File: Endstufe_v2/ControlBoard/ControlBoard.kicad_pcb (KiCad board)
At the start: 2 copper layers, 216 parts, among them J1 B4B-XH-2_(LF)(SN), J10 DNP, J11 DNP, J12 DNP, J13 DNP, J14 DAC all outputs, J2 B4B-XH-2_(LF)(SN), J3 B4B-XH-2_(LF)(SN), J4 DNP, J5 B6B-XH-2(LF)(SN), J6 Conn_01x02_Pin, J7 DNP, J8 DNP, J9 DNP, SW1 TS-1187A-B-A-B, SW2 TS-1187A-B-A-B, U1 NVTFWS014P04M8LTAG, U10 ADAU1962AWBSTZ, U2 1SMA5927A, U3 TPS62933, U4 TYPE-C 16PFS 2JCB1.2-H6.5 IPX8, U5 W25Q128JVS, U6 RP2040, U7 W25Q128JVS, U8 ADAU1463WBCPZ300, U9 ZPLR135_T8, Y1 12Mhz, Y2 24.576Mhz, Y3 24.576Mhz

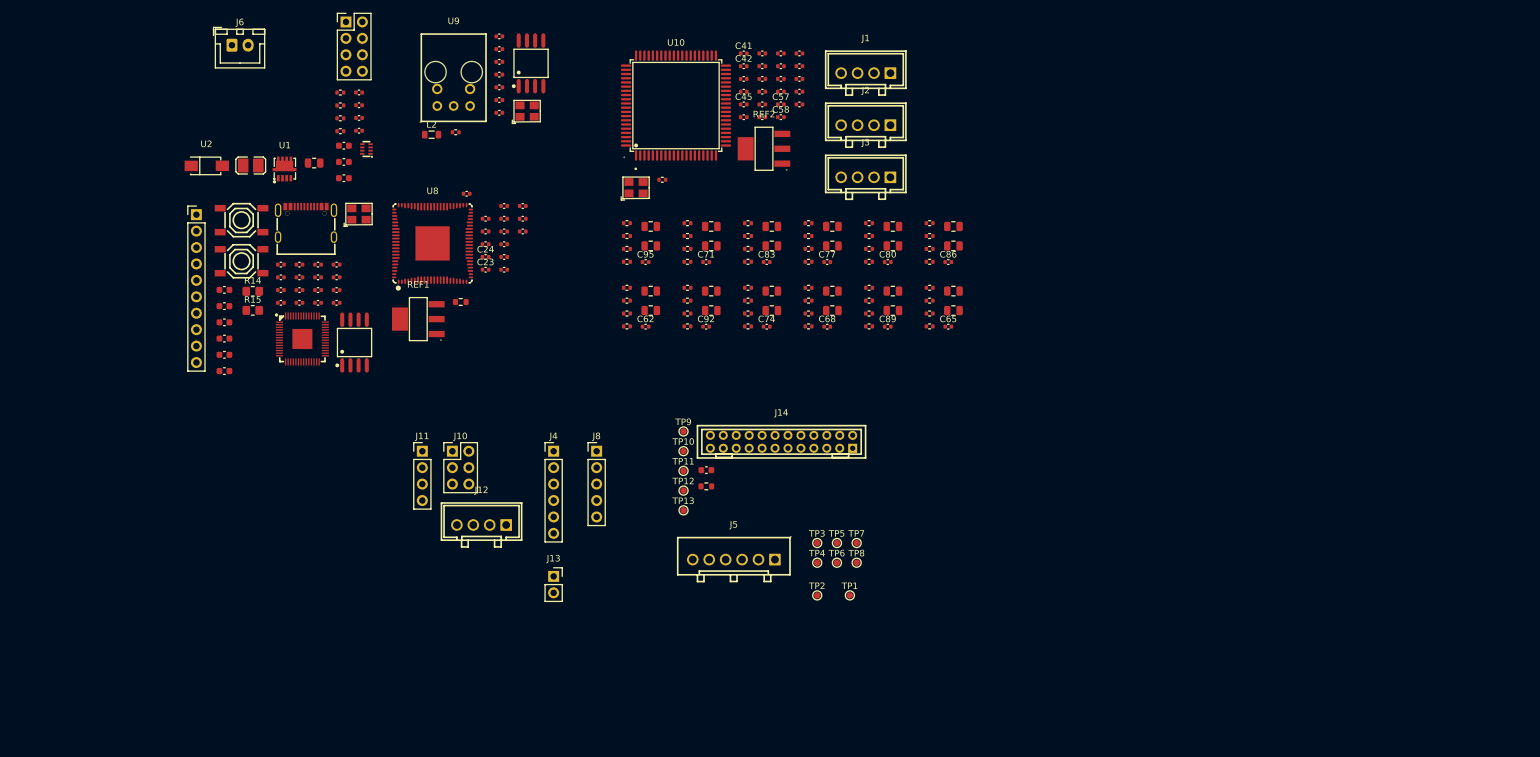
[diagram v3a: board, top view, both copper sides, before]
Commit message: Rough layout of components
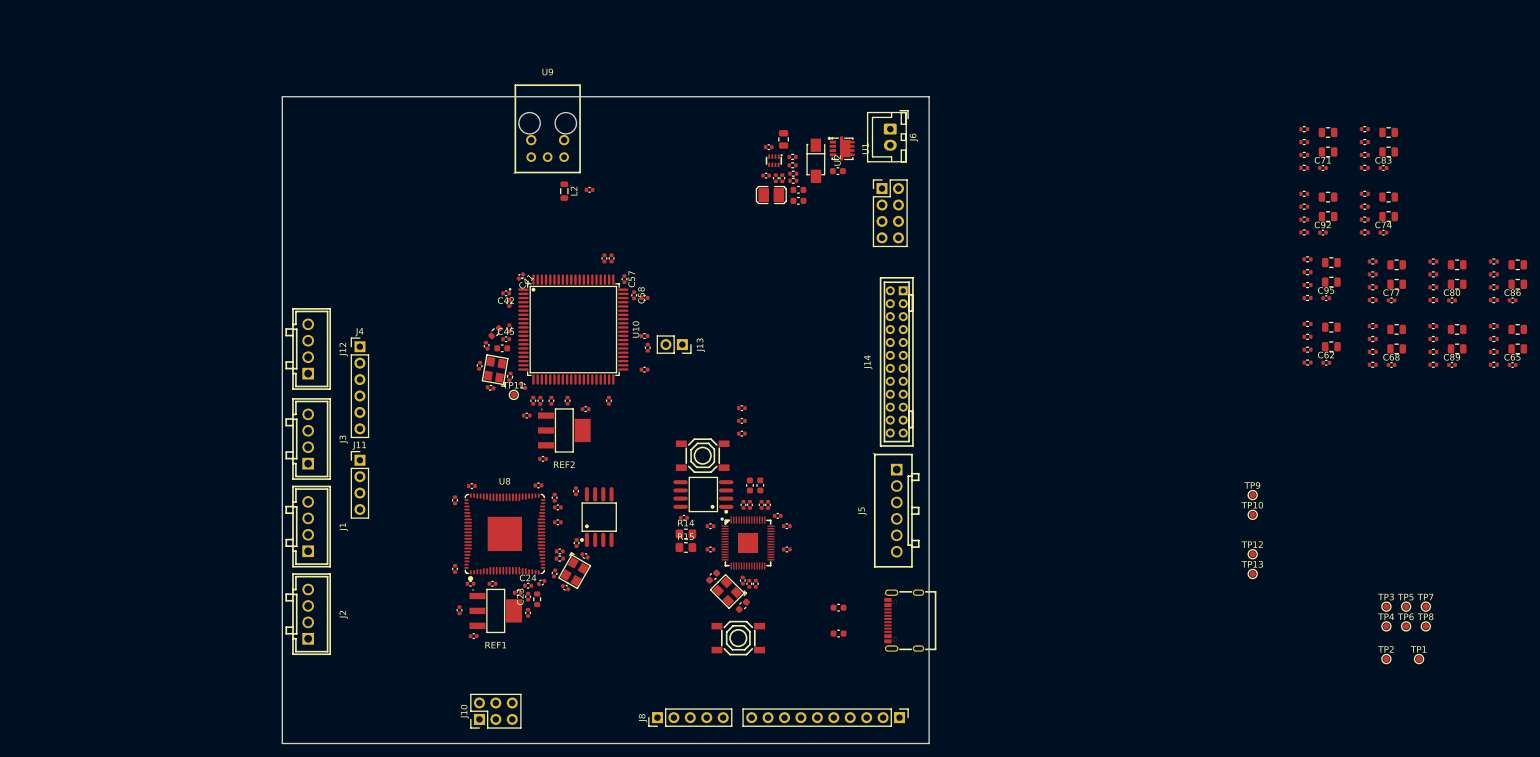
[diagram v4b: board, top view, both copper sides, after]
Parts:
- added C100: 10uF, Endstufe:C_0402_1005Metric, F.Cu at (110.3, 126.0)
- added C98: 10uF, Endstufe:C_0402_1005Metric, F.Cu at (116.9, 118.3)
- added C99: 10uF, Endstufe:C_0402_1005Metric, F.Cu at (99.6, 153.4)
- moved J9 133.7 mm to (165.4, 166.0), turned to -90 degrees
- moved J2 114.7 mm to (74.0, 150.0), turned to -90 degrees
- moved J1 111.1 mm to (74.0, 136.5), turned to -90 degrees
- moved U4 111.0 mm to (166.0, 151.0), turned to 90 degrees
- moved C62 105.4 mm to (231.4, 111.1)
- moved C63 105.4 mm to (232.2, 105.6)
- moved C64 105.4 mm to (232.2, 108.7)
- moved C95 105.4 mm to (231.4, 101.2)
- moved C96 105.4 mm to (232.2, 95.7)
- moved C97 105.4 mm to (232.2, 98.7)
- moved R26 105.4 mm to (228.5, 105.1)
- moved R27 105.4 mm to (228.5, 107.1)
- moved R28 105.4 mm to (228.5, 109.1)
- moved R29 105.4 mm to (228.5, 111.1)
- moved R70 105.4 mm to (228.5, 95.1)
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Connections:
- J1 pad 2: /ADAU1463/PCM9211_BLCK -> /ADAU1463/PCM9211_LRCLK
- J1 pad 3: /ADAU1463/PCM9211_LRCLK -> /ADAU1463/PCM9211_BLCK
- J2 pad 2: /ADAU1463/PCM1865_BLCK -> /ADAU1463/PCM1865_LRCLK
- J2 pad 3: /ADAU1463/PCM1865_LRCLK -> /ADAU1463/PCM1865_BLCK
- J3 pad 2: /ADAU1463/ADDITIONAL_BLCK -> /ADAU1463/ADDITIONAL_LRCLK
- J3 pad 3: /ADAU1463/ADDITIONAL_LRCLK -> /ADAU1463/ADDITIONAL_BLCK
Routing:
- added copper zone on In1.Cu, net GND
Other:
- board outline added: 100 x 100 mm
- copper layers 2 -> 4

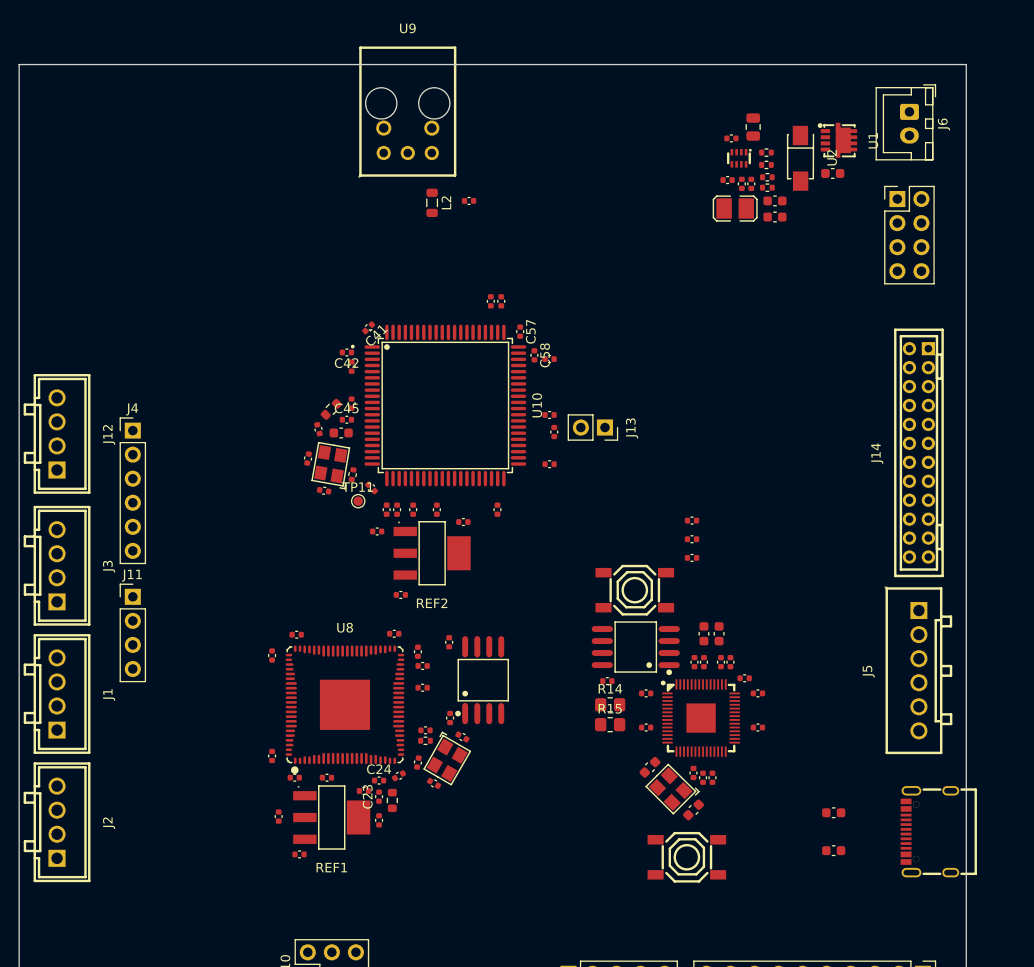
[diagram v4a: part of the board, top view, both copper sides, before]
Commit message: Layout amplifier board
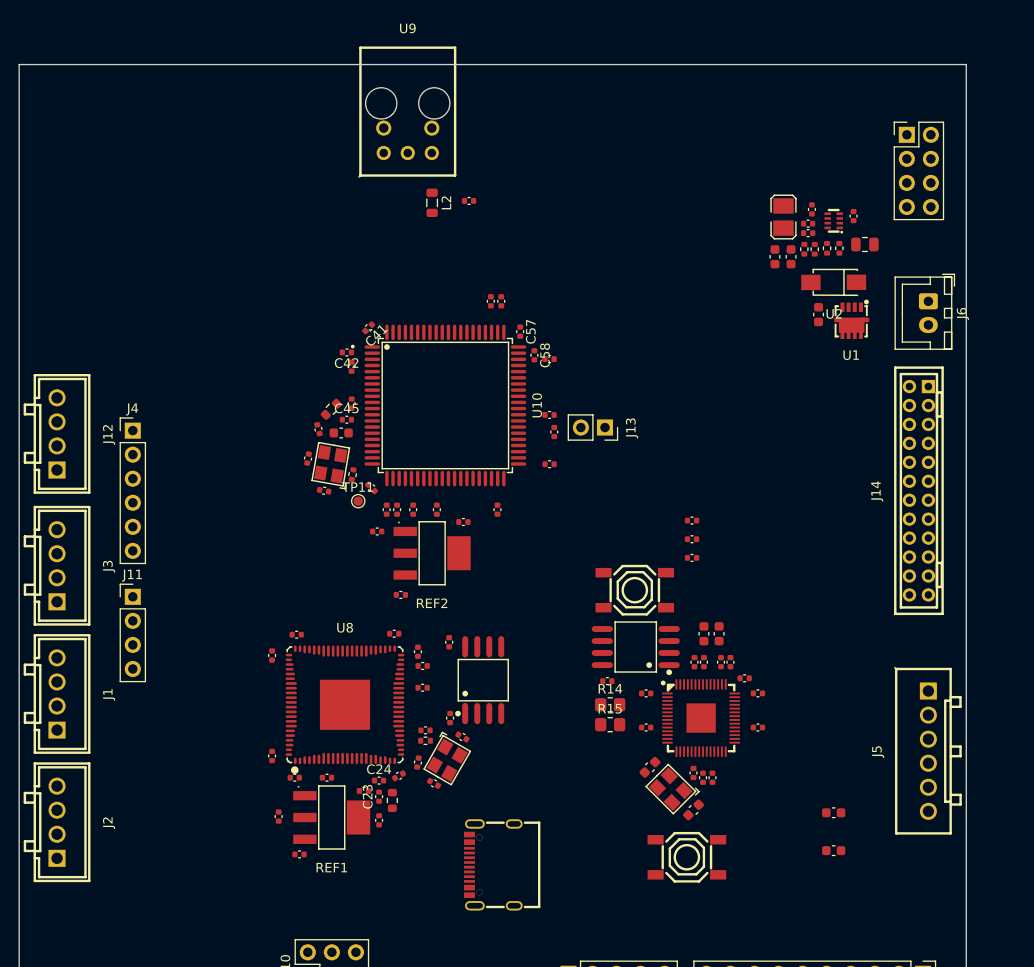
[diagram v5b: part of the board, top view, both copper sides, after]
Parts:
- moved U4 46.2 mm to (119.9, 154.5)
- moved J6 20.1 mm to (166.0, 95.0)
- moved U1 19.2 mm to (157.9, 97.1), turned to 180 degrees
- moved C1 17.1 mm to (159.3, 89.0), turned to 0 degrees
- moved C2 15.3 mm to (158.1, 86.0), turned to 90 degrees
- moved R2 15.0 mm to (154.4, 96.4), turned to -90 degrees
- moved U2 13.6 mm to (156.0, 93.0), turned to 180 degrees
- moved R1 12.7 mm to (156.6, 89.4), turned to -90 degrees
- moved U3 12.0 mm to (156.0, 86.5), turned to 0 degrees
- moved R5 10.9 mm to (155.3, 89.4), turned to -90 degrees
- moved C4 9.42 mm to (153.7, 85.3), turned to 90 degrees
- moved R4 9.10 mm to (154.0, 89.5), turned to 90 degrees
- moved J5 8.56 mm to (166.0, 142.5)
- moved C3 8.16 mm to (153.3, 86.8), turned to 180 degrees
- moved C5 7.94 mm to (153.3, 87.8), turned to 0 degrees
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
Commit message: Continue layouting
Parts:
- added J15: B4B-XH-2_(LF)(SN), Endstufe:CONN-TH_B4B-XH-2-LF-SN, F.Cu at (117.7, 151.0)
- added J16: B6B-XH-2(LF)(SN), Endstufe:CONN-TH_B6B-XH-2-LF-SN, F.Cu at (153.0, 151.0)
- U8: value ADAU1463WBCPZ300 -> ADAU1467WBCPZ300
- moved J9 57.5 mm to (189.0, 113.6), turned to 0 degrees
- moved J8 32.5 mm to (152.0, 144.0), turned to 180 degrees
- moved R8 31.6 mm to (186.0, 143.0)
- moved R7 30.1 mm to (186.0, 146.0)
- moved SW2 22.9 mm to (158.0, 139.0), turned to 90 degrees
- moved U4 11.8 mm to (131.0, 150.4), turned to 0 degrees
- moved J14 2.24 mm to (166.0, 117.0)
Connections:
- net /ADAU1463/ADDITIONAL_BLCK renamed /ADAU1467/ADDITIONAL_BLCK
- net /ADAU1463/ADDITIONAL_LRCLK renamed /ADAU1467/ADDITIONAL_LRCLK
- net /ADAU1463/ADDITIONAL_SDATA renamed /ADAU1467/ADDITIONAL_SDATA
- net /ADAU1463/ADDR0 renamed /ADAU1467/ADDR0
- net /ADAU1463/ADDR1 renamed /ADAU1467/ADDR1
- net /ADAU1463/AUXADC0 renamed /ADAU1467/AUXADC0
- net /ADAU1463/AUXADC1 renamed /ADAU1467/AUXADC1
- net /ADAU1463/DAC_BLCK renamed /ADAU1467/DAC_BLCK
- net /ADAU1463/DAC_DATA0 renamed /ADAU1467/DAC_DATA0
- net /ADAU1463/DAC_DATA1 renamed /ADAU1467/DAC_DATA1
- net /ADAU1463/DAC_DATA2 renamed /ADAU1467/DAC_DATA2
- net /ADAU1463/DAC_LRCLK renamed /ADAU1467/DAC_LRCLK
- net /ADAU1463/PCM1865_BLCK renamed /ADAU1467/PCM1865_BLCK
- net /ADAU1463/PCM1865_LRCLK renamed /ADAU1467/PCM1865_LRCLK
- net /ADAU1463/PCM1865_SDATA renamed /ADAU1467/PCM1865_SDATA
- net /ADAU1463/PCM9211_BLCK renamed /ADAU1467/PCM9211_BLCK
- net /ADAU1463/PCM9211_LRCLK renamed /ADAU1467/PCM9211_LRCLK
- net /ADAU1463/PCM9211_SDATA renamed /ADAU1467/PCM9211_SDATA
- net /ADAU1463/SPDIFIN renamed /ADAU1467/SPDIFIN
- net /ADAU1463/SPI_MISO renamed /ADAU1467/SPI_MISO
- net /ADAU1463/SPI_MOSI renamed /ADAU1467/SPI_MOSI
- net /ADAU1463/SPI_SCLK renamed /ADAU1467/SPI_SCLK
- net /ADAU1463/SPI_SS renamed /ADAU1467/SPI_SS
- J13 pad 2: /ADAU1962A/RESET -> /ADAU1962A_RESET
- R14 pad 2: /RP2040/GPIO0_I2C0_SDA -> /SDA
- R15 pad 2: /RP2040/GPIO1_I2C0_SCL -> /SCL
- R20 pad 2: /ADAU1463/RESET -> /ADAU1467_RESET
- R25 pad 1: /ADAU1962A/RESET -> /ADAU1962A_RESET
- U10 pad 43: /ADAU1962A/SDA -> /SDA
- U10 pad 44: /ADAU1962A/SCL -> /SCL
- U10 pad 47: /ADAU1962A/RESET -> /ADAU1962A_RESET
- U6 pad 11: /RP2040/GPIO8 -> /PCM9211_RST
- U6 pad 12: /RP2040/GPIO9 -> /ADAU1467_RESET
- U6 pad 13: unconnected-(U6-GPIO10-Pad13) -> /ADAU1962A_RESET
- U6 pad 2: /RP2040/GPIO0_I2C0_SDA -> /SDA
- U6 pad 3: /RP2040/GPIO1_I2C0_SCL -> /SCL
- U6 pad 4: /RP2040/GPIO2 -> /SDZA
- U6 pad 5: /RP2040/GPIO3 -> /SDZB
- U6 pad 6: /RP2040/GPIO4 -> /FAULTZA
- U6 pad 7: /RP2040/GPIO5 -> /FAULTZB
- U6 pad 8: /RP2040/GPIO6 -> /MUTEA
- U6 pad 9: /RP2040/GPIO7 -> /MUTEB
- U8 pad 28: /ADAU1463/RESET -> /ADAU1467_RESET
- U8 pad 38: /ADAU1463/SDA -> /SDA
- U8 pad 39: /ADAU1463/SCL -> /SCL

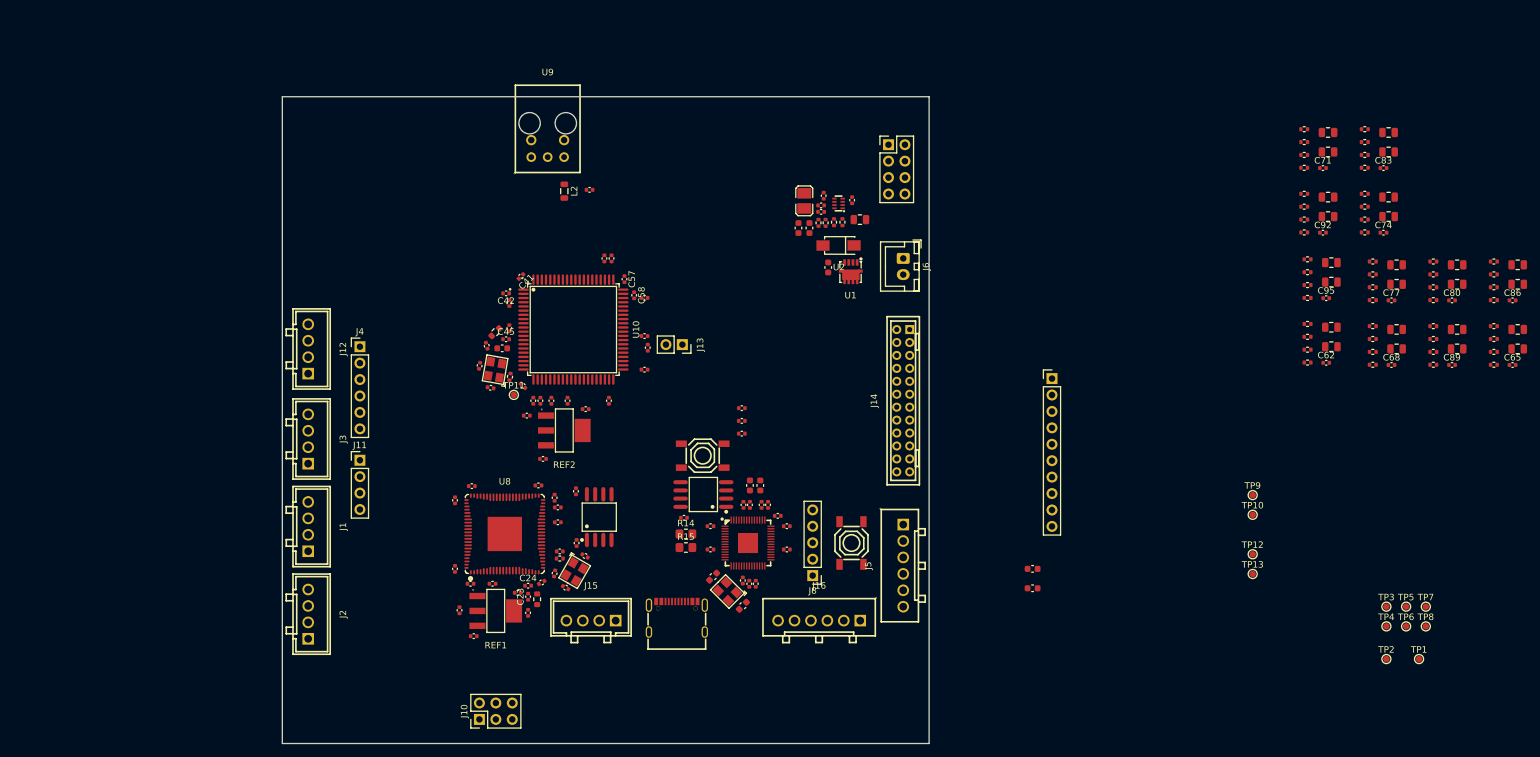
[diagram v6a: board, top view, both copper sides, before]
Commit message: Make mounting holes and continue layouting
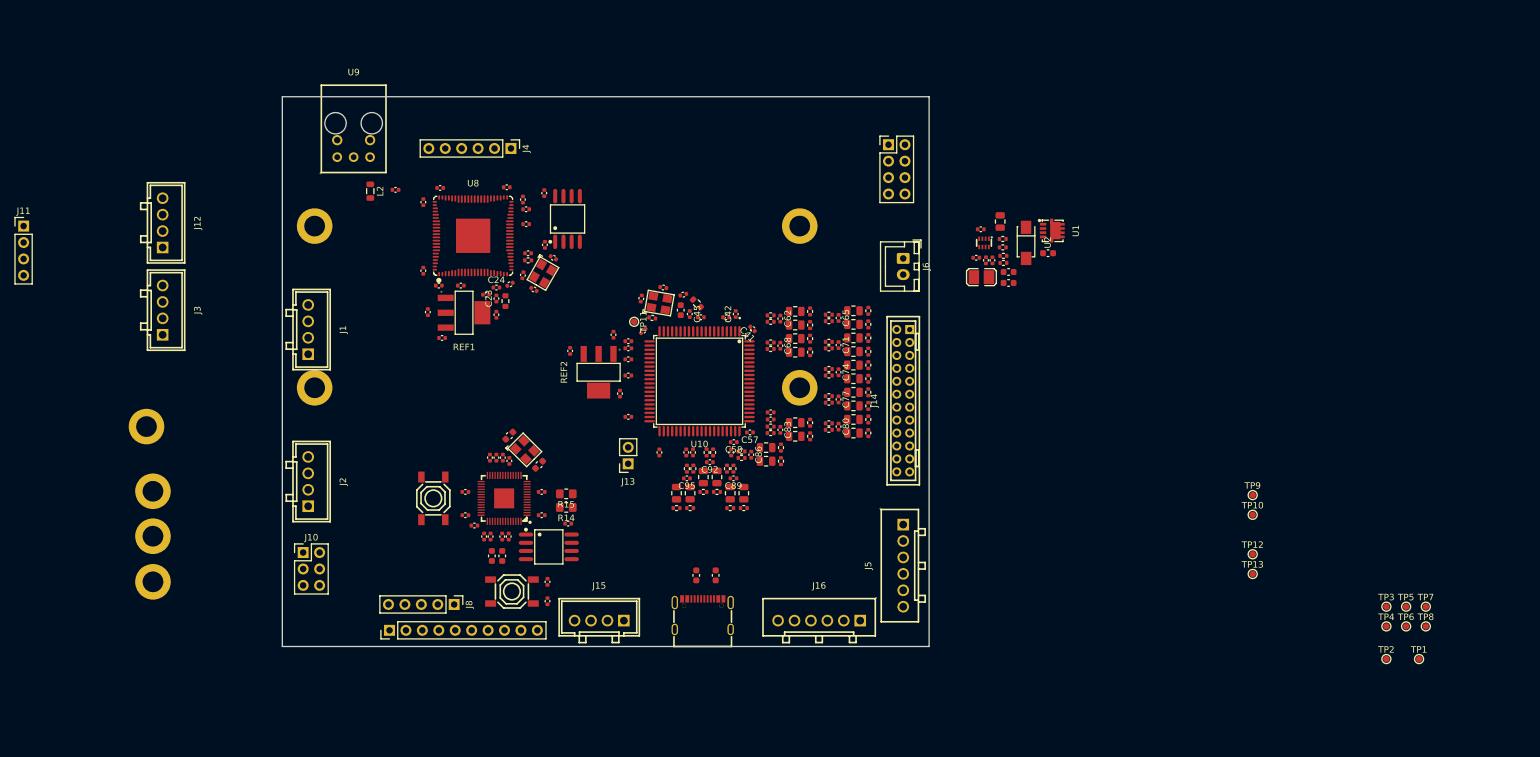
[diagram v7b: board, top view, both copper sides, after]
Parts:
- added H1: MountingHole_Pad, Endstufe:MountingHole_3.2mm_M3_ISO14580_Pad, F.Cu at (75.0, 90.0)
- added H2: MountingHole_Pad, Endstufe:MountingHole_3.2mm_M3_ISO14580_Pad, F.Cu at (150.0, 90.0)
- added H3: MountingHole_Pad, Endstufe:MountingHole_3.2mm_M3_ISO14580_Pad, F.Cu at (75.0, 115.0)
- added H4: MountingHole_Pad, Endstufe:MountingHole_3.2mm_M3_ISO14580_Pad, F.Cu at (150.0, 115.0)
- added H5: MountingHole_Pad, Endstufe:MountingHole_3.2mm_M3_ISO14580_Pad, F.Cu at (50.0, 131.0)
- added H6: MountingHole_Pad, Endstufe:MountingHole_3.2mm_M3_ISO14580_Pad, F.Cu at (49.0, 121.0)
- added H7: MountingHole_Pad, Endstufe:MountingHole_3.2mm_M3_ISO14580_Pad, F.Cu at (50.0, 137.9)
- added H8: MountingHole_Pad, Endstufe:MountingHole_3.2mm_M3_ISO14580_Pad, F.Cu at (50.0, 145.0)
- moved R58 120.2 mm to (141.0, 125.9)
- moved C86 120.1 mm to (142.5, 125.4), turned to -90 degrees
- moved C87 120.1 mm to (144.8, 126.3)
- moved R59 119.5 mm to (141.0, 124.9)
- moved C88 118.9 mm to (144.8, 124.2), turned to 180 degrees
- moved C90 115.2 mm to (139.2, 131.3), turned to -90 degrees
- moved R60 113.5 mm to (147.1, 126.3), turned to 90 degrees
- moved R61 112.6 mm to (147.1, 124.2), turned to -90 degrees
- moved C91 112.5 mm to (141.3, 131.3), turned to 90 degrees
- moved C89 112.5 mm to (139.8, 129.0), turned to 180 degrees
- moved R62 111.4 mm to (138.7, 127.5), turned to -90 degrees
- moved R64 111.4 mm to (139.2, 133.6)
- moved R63 110.1 mm to (139.7, 127.5), turned to -90 degrees
- moved J9 109.6 mm to (86.6, 152.5), turned to 90 degrees
- moved R65 108.9 mm to (141.3, 133.6), turned to 180 degrees
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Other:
- board size 100 x 100 mm -> 100 x 85 mm
